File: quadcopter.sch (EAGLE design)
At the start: 69 parts, among them J1 AVR_SPI_PRG_6NS, U1 ATMEGA128RFA1, Y2 16MHz

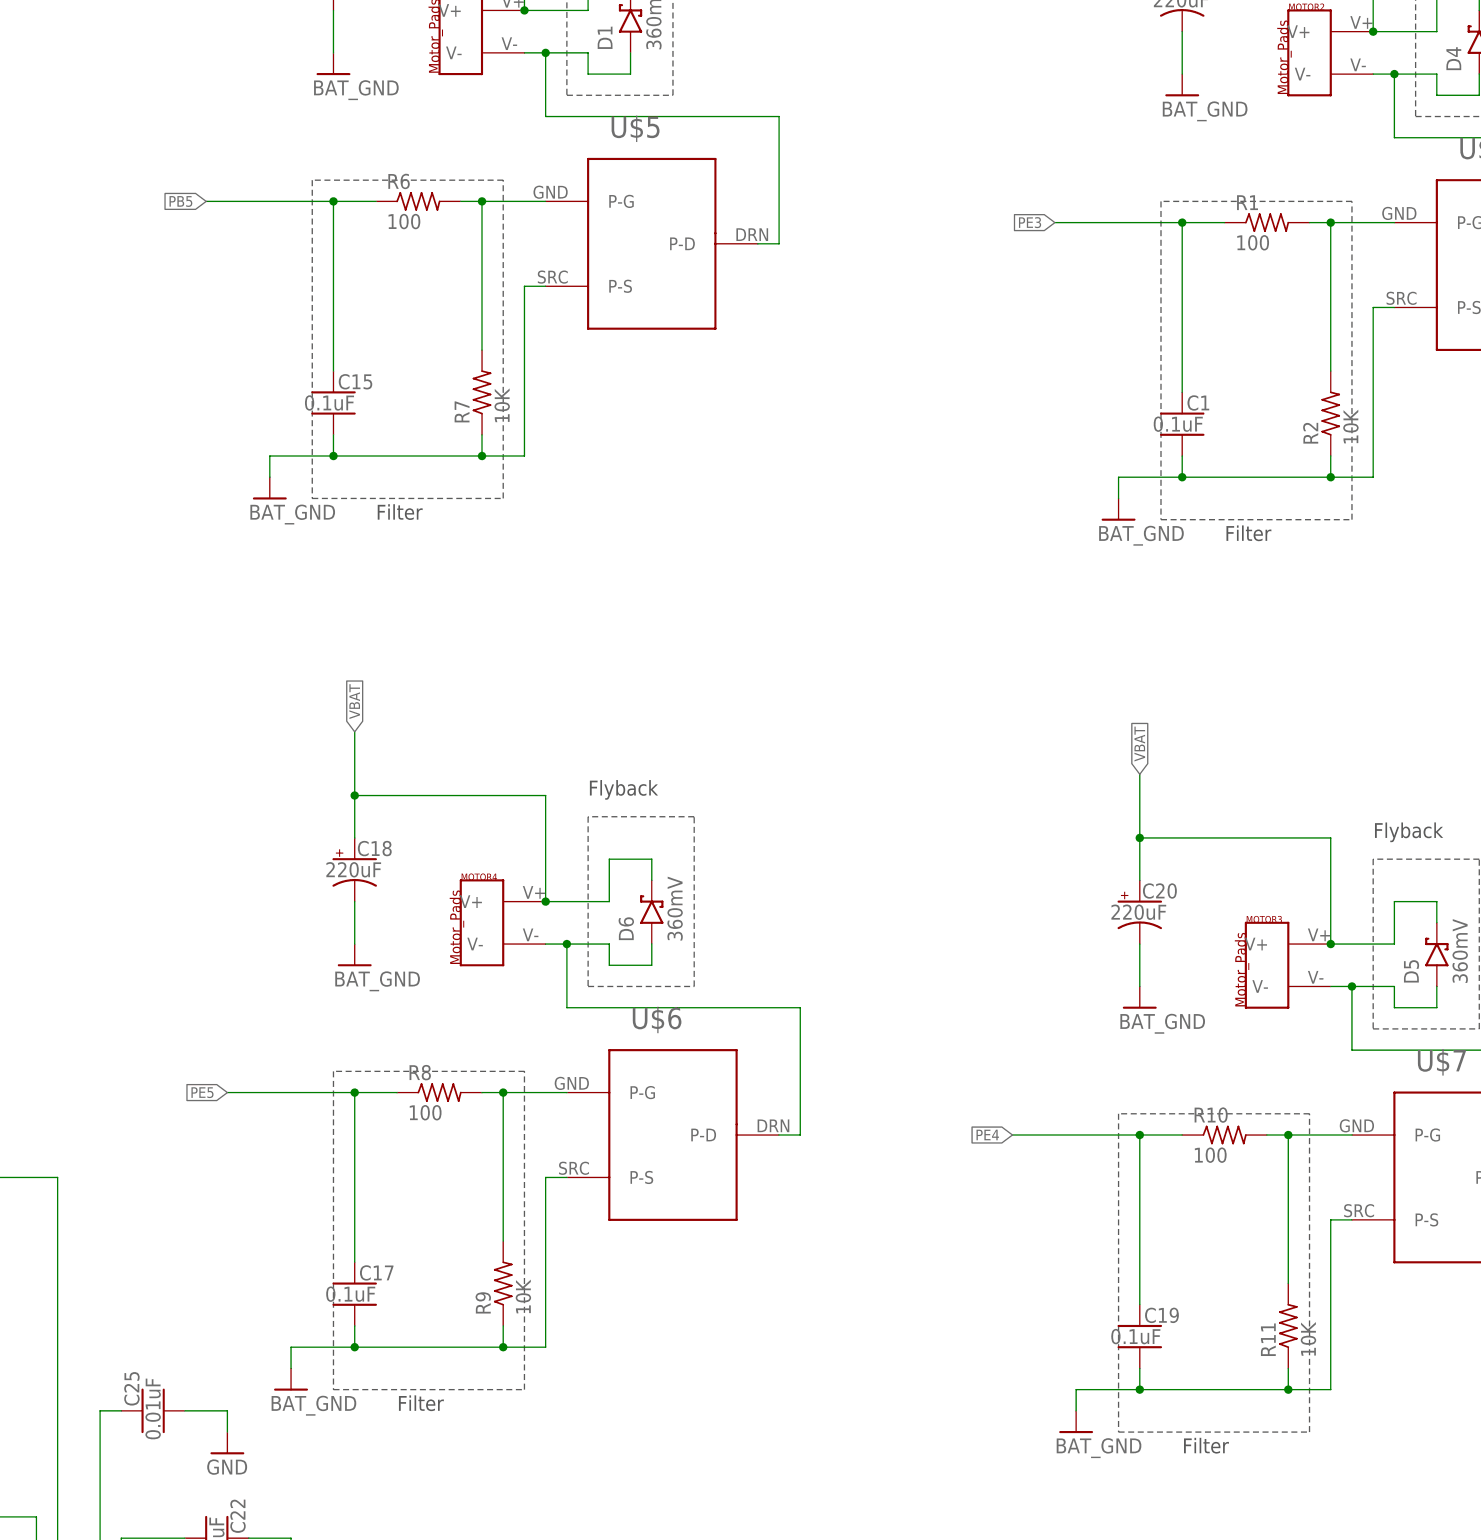
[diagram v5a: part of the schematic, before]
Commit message: Manually routed crystal, fixed motor driver filters.
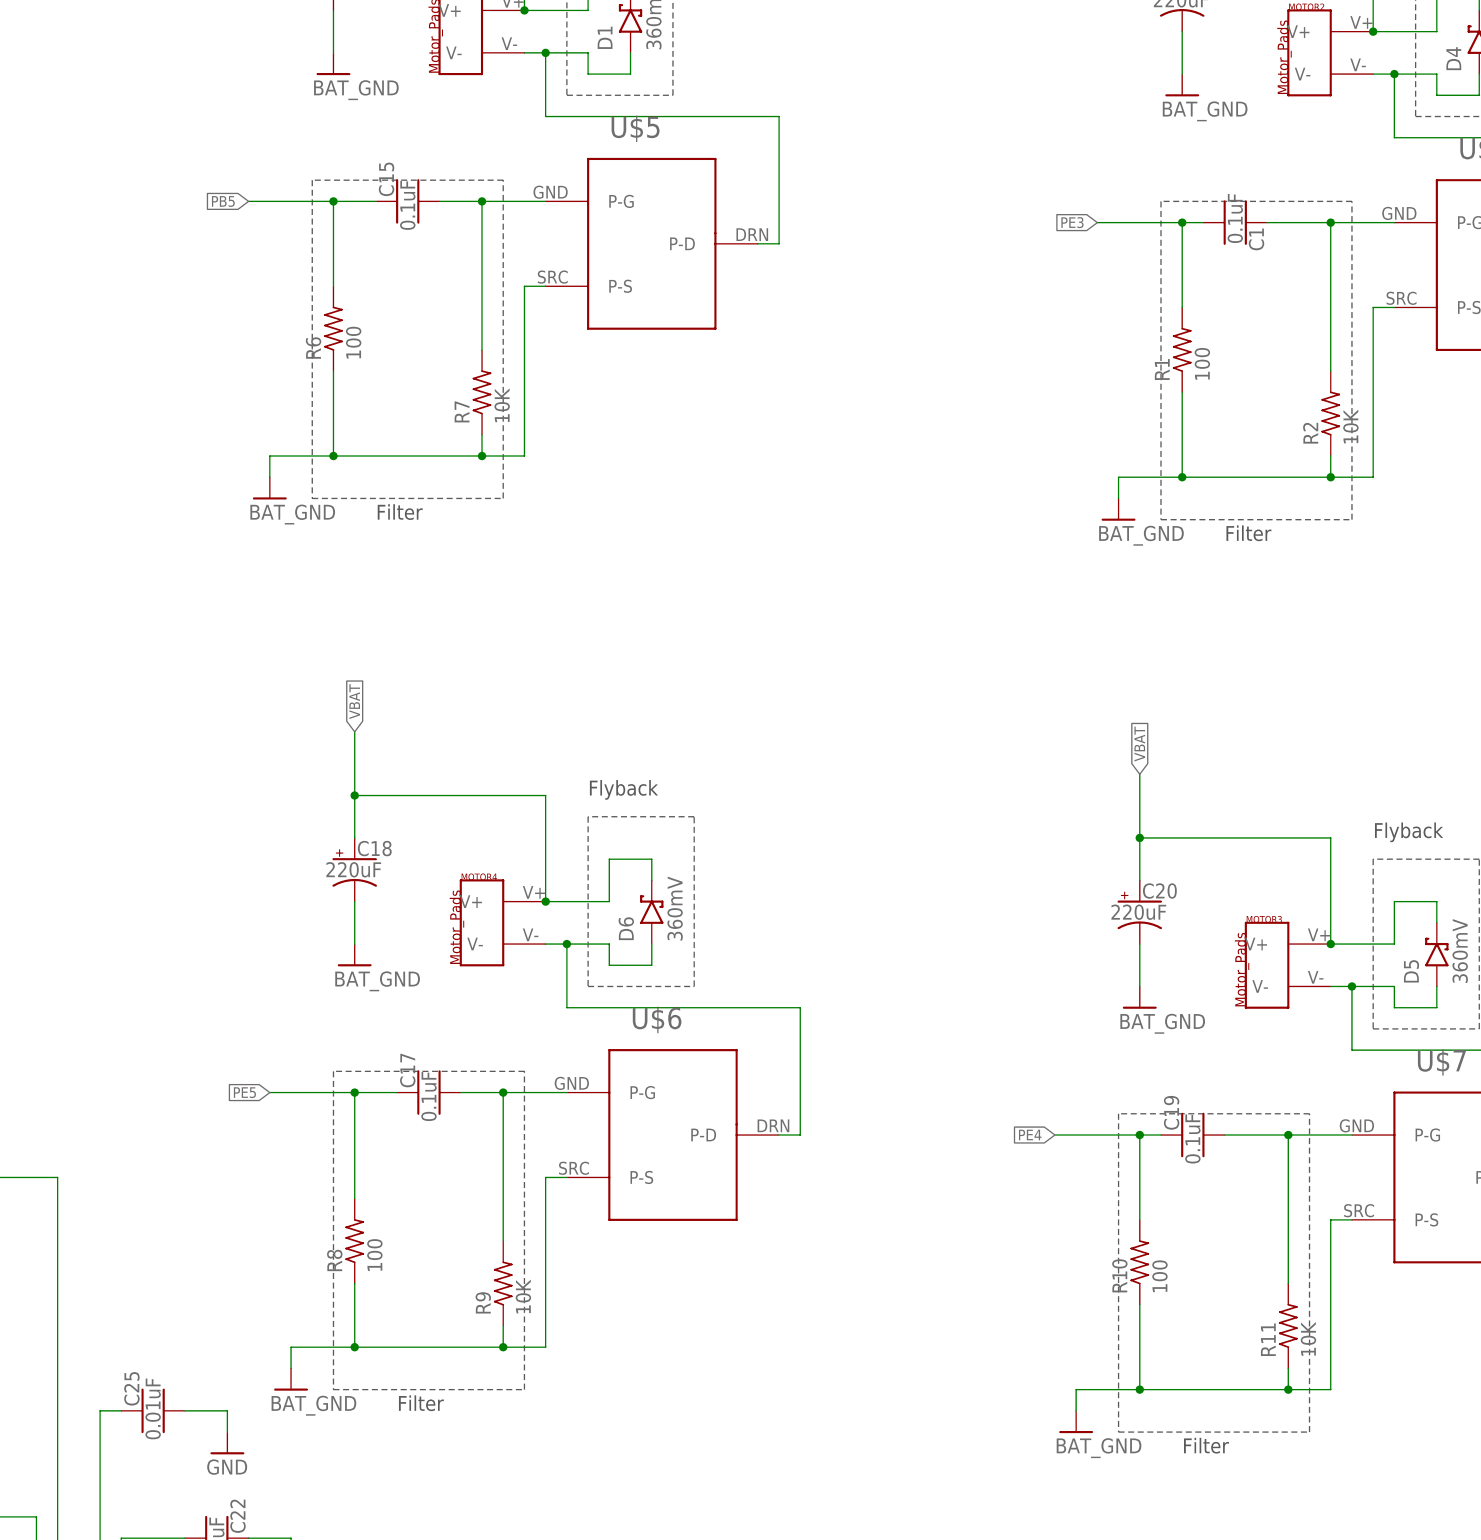
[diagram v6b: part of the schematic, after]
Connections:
- net BAT_GND: now also R1.1, R10.1, R6.1, R8.1; no longer C1.2, C15.2, C17.2, C19.2
- net FILTERED1: now also C15.2; no longer R6.2
- net FILTERED2: now also C1.1; no longer R1.2
- net FILTERED3: now also C19.2; no longer R10.2
- net FILTERED4: now also C17.2; no longer R8.2
- net PB5: now also R6.2; no longer R6.1
- net PE3: now also C1.2, R1.2; no longer C1.1, R1.1
- net PE4: now also R10.2; no longer R10.1
- net PE5: now also R8.2; no longer R8.1
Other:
- moved on the sheet: C1, C15, C17, C19, R1, R10, R6, R8
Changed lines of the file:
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@@
 </plain>
 <instances>
-<instance part="R1" gate="G$1" x="373.38" y="215.9"/>
+<instance part="R1" gate="G$1" x="363.22" y="200.66" rot="R90"/>
 <instance part="R2" gate="G$1" x="381" y="193.04" rot="R90"/>
 <instance part="GND1" gate="1" x="363.22" y="231.14"/>
@@
 <instance part="J2" gate="G$1" x="132.08" y="231.14"/>
 <instance part="J3" gate="G$1" x="63.5" y="251.46" rot="R270"/>
-<instance part="R6" gate="G$1" x="271.78" y="218.44"/>
+<instance part="R6" gate="G$1" x="261.62" y="203.2" rot="R90"/>
 <instance part="R7" gate="G$1" x="279.4" y="195.58" rot="R90"/>
 <instance part="GND27" gate="1" x="261.62" y="233.68"/>
@@
 <instance part="GND28" gate="1" x="254" y="182.88"/>
 <instance part="U$5" gate="G$1" x="299.72" y="213.36"/>
-<instance part="R8" gate="G$1" x="274.32" y="111.76"/>
+<instance part="R8" gate="G$1" x="264.16" y="93.98" rot="R90"/>
 <instance part="R9" gate="G$1" x="281.94" y="88.9" rot="R90"/>
 <instance part="GND29" gate="1" x="264.16" y="127"/>
@@
 <instance part="GND30" gate="1" x="256.54" y="76.2"/>
 <instance part="U$6" gate="G$1" x="302.26" y="106.68"/>
-<instance part="R10" gate="G$1" x="368.3" y="106.68"/>
+<instance part="R10" gate="G$1" x="358.14" y="91.44" rot="R90"/>
 <instance part="R11" gate="G$1" x="375.92" y="83.82" rot="R90"/>
 <instance part="GND31" gate="1" x="358.14" y="121.92"/>
@@
 <instance part="C25" gate="G$1" x="238.76" y="73.66" rot="R90"/>
 <instance part="C22" gate="G$1" x="248.92" y="58.42" rot="MR90"/>
-<instance part="C15" gate="G$1" x="261.62" y="195.58"/>
-<instance part="C1" gate="G$1" x="363.22" y="193.04"/>
-<instance part="C17" gate="G$1" x="264.16" y="88.9"/>
-<instance part="C19" gate="G$1" x="358.14" y="83.82"/>
+<instance part="C15" gate="G$1" x="269.24" y="218.44" rot="R90"/>
+<instance part="C1" gate="G$1" x="370.84" y="215.9" rot="R270"/>
+<instance part="C17" gate="G$1" x="271.78" y="111.76" rot="R90"/>
+<instance part="C19" gate="G$1" x="363.22" y="106.68" rot="R90"/>
 </instances>
 <busses>
@@
 <pinref part="R9" gate="G$1" pin="2"/>
 <wire x1="281.94" y1="93.98" x2="281.94" y2="111.76" width="0.1524" layer="91"/>
-<pinref part="R8" gate="G$1" pin="2"/>
-<wire x1="279.4" y1="111.76" x2="281.94" y2="111.76" width="0.1524" layer="91"/>
+<pinref part="C17" gate="G$1" pin="2"/>
+<wire x1="276.86" y1="111.76" x2="281.94" y2="111.76" width="0.1524" layer="91"/>
 <junction x="281.94" y="111.76"/>
 </segment>
@@
 </segment>
 <segment>
-<wire x1="261.62" y1="198.12" x2="261.62" y2="218.44" width="0.1524" layer="91"/>
-<pinref part="R6" gate="G$1" pin="1"/>
-<wire x1="266.7" y1="218.44" x2="261.62" y2="218.44" width="0.1524" layer="91"/>
+<pinref part="R6" gate="G$1" pin="2"/>
+<wire x1="261.62" y1="208.28" x2="261.62" y2="218.44" width="0.1524" layer="91"/>
+<pinref part="C15" gate="G$1" pin="1"/>
+<wire x1="261.62" y1="218.44" x2="266.7" y2="218.44" width="0.1524" layer="91"/>
+<wire x1="261.62" y1="218.44" x2="251.46" y2="218.44" width="0.1524" layer="91"/>
 <junction x="261.62" y="218.44"/>
-<wire x1="261.62" y1="218.44" x2="246.38" y2="218.44" width="0.1524" layer="91"/>
-<label x="246.38" y="218.44" size="1.27" layer="95" rot="R180" xref="yes"/>
-<pinref part="C15" gate="G$1" pin="1"/>
+<label x="251.46" y="218.44" size="1.27" layer="95" rot="R180" xref="yes"/>
 </segment>
 </net>
@@
 </segment>
 <segment>
-<wire x1="363.22" y1="195.58" x2="363.22" y2="215.9" width="0.1524" layer="91"/>
-<pinref part="R1" gate="G$1" pin="1"/>
-<wire x1="368.3" y1="215.9" x2="363.22" y2="215.9" width="0.1524" layer="91"/>
+<pinref part="R1" gate="G$1" pin="2"/>
+<wire x1="363.22" y1="205.74" x2="363.22" y2="215.9" width="0.1524" layer="91"/>
+<pinref part="C1" gate="G$1" pin="2"/>
+<wire x1="363.22" y1="215.9" x2="365.76" y2="215.9" width="0.1524" layer="91"/>
+<wire x1="363.22" y1="215.9" x2="353.06" y2="215.9" width="0.1524" layer="91"/>
 <junction x="363.22" y="215.9"/>
-<wire x1="363.22" y1="215.9" x2="347.98" y2="215.9" width="0.1524" layer="91"/>
-<label x="347.98" y="215.9" size="1.27" layer="95" rot="R180" xref="yes"/>
-<pinref part="C1" gate="G$1" pin="1"/>
+<label x="353.06" y="215.9" size="1.27" layer="95" rot="R180" xref="yes"/>
 </segment>
 </net>
@@
 </segment>
 <segment>
-<wire x1="358.14" y1="86.36" x2="358.14" y2="106.68" width="0.1524" layer="91"/>
-<pinref part="R10" gate="G$1" pin="1"/>
-<wire x1="363.22" y1="106.68" x2="358.14" y2="106.68" width="0.1524" layer="91"/>
+<pinref part="R10" gate="G$1" pin="2"/>
+<wire x1="358.14" y1="96.52" x2="358.14" y2="106.68" width="0.1524" layer="91"/>
+<pinref part="C19" gate="G$1" pin="1"/>
+<wire x1="358.14" y1="106.68" x2="360.68" y2="106.68" width="0.1524" layer="91"/>
+<wire x1="358.14" y1="106.68" x2="347.98" y2="106.68" width="0.1524" layer="91"/>
 <junction x="358.14" y="106.68"/>
-<wire x1="358.14" y1="106.68" x2="342.9" y2="106.68" width="0.1524" layer="91"/>
-<label x="342.9" y="106.68" size="1.27" layer="95" rot="R180" xref="yes"/>
-<pinref part="C19" gate="G$1" pin="1"/>
+<label x="347.98" y="106.68" size="1.27" layer="95" rot="R180" xref="yes"/>
 </segment>
 </net>
@@
 </segment>
 <segment>
-<wire x1="264.16" y1="91.44" x2="264.16" y2="111.76" width="0.1524" layer="91"/>
-<pinref part="R8" gate="G$1" pin="1"/>
+<pinref part="C17" gate="G$1" pin="1"/>
 <wire x1="269.24" y1="111.76" x2="264.16" y2="111.76" width="0.1524" layer="91"/>
+<pinref part="R8" gate="G$1" pin="2"/>
+<wire x1="264.16" y1="111.76" x2="254" y2="111.76" width="0.1524" layer="91"/>
+<wire x1="264.16" y1="111.76" x2="264.16" y2="99.06" width="0.1524" layer="91"/>
 <junction x="264.16" y="111.76"/>
-<wire x1="264.16" y1="111.76" x2="248.92" y2="111.76" width="0.1524" layer="91"/>
-<label x="248.92" y="111.76" size="1.27" layer="95" rot="R180" xref="yes"/>
-<pinref part="C17" gate="G$1" pin="1"/>
+<label x="254" y="111.76" size="1.27" layer="95" rot="R180" xref="yes"/>
 </segment>
 </net>
@@
 <pinref part="R9" gate="G$1" pin="1"/>
 <wire x1="281.94" y1="83.82" x2="281.94" y2="81.28" width="0.1524" layer="91"/>
-<wire x1="264.16" y1="81.28" x2="264.16" y2="83.82" width="0.1524" layer="91"/>
+<junction x="281.94" y="81.28"/>
+<pinref part="R8" gate="G$1" pin="1"/>
+<wire x1="264.16" y1="88.9" x2="264.16" y2="81.28" width="0.1524" layer="91"/>
 <junction x="264.16" y="81.28"/>
-<pinref part="C17" gate="G$1" pin="2"/>
-<junction x="281.94" y="81.28"/>
 </segment>
 <segment>
@@
 <pinref part="R7" gate="G$1" pin="1"/>
 <wire x1="279.4" y1="190.5" x2="279.4" y2="187.96" width="0.1524" layer="91"/>
-<wire x1="261.62" y1="187.96" x2="261.62" y2="190.5" width="0.1524" layer="91"/>
+<junction x="279.4" y="187.96"/>
+<pinref part="R6" gate="G$1" pin="1"/>
+<wire x1="261.62" y1="198.12" x2="261.62" y2="187.96" width="0.1524" layer="91"/>
 <junction x="261.62" y="187.96"/>
-<pinref part="C15" gate="G$1" pin="2"/>
-<junction x="279.4" y="187.96"/>
 </segment>
 <segment>
@@
 <pinref part="R11" gate="G$1" pin="1"/>
 <wire x1="375.92" y1="78.74" x2="375.92" y2="76.2" width="0.1524" layer="91"/>
-<wire x1="358.14" y1="76.2" x2="358.14" y2="78.74" width="0.1524" layer="91"/>
+<junction x="375.92" y="76.2"/>
+<pinref part="R10" gate="G$1" pin="1"/>
+<wire x1="358.14" y1="86.36" x2="358.14" y2="76.2" width="0.1524" layer="91"/>
 <junction x="358.14" y="76.2"/>
-<pinref part="C19" gate="G$1" pin="2"/>
-<junction x="375.92" y="76.2"/>
 </segment>
 <segment>
@@
 <pinref part="R2" gate="G$1" pin="1"/>
 <wire x1="381" y1="187.96" x2="381" y2="185.42" width="0.1524" layer="91"/>
-<wire x1="363.22" y1="185.42" x2="363.22" y2="187.96" width="0.1524" layer="91"/>
+<junction x="381" y="185.42"/>
+<pinref part="R1" gate="G$1" pin="1"/>
+<wire x1="363.22" y1="195.58" x2="363.22" y2="185.42" width="0.1524" layer="91"/>
 <junction x="363.22" y="185.42"/>
-<pinref part="C1" gate="G$1" pin="2"/>
-<junction x="381" y="185.42"/>
 </segment>
 <segment>
@@
 <pinref part="R7" gate="G$1" pin="2"/>
 <wire x1="279.4" y1="200.66" x2="279.4" y2="218.44" width="0.1524" layer="91"/>
-<pinref part="R6" gate="G$1" pin="2"/>
-<wire x1="276.86" y1="218.44" x2="279.4" y2="218.44" width="0.1524" layer="91"/>
+<pinref part="C15" gate="G$1" pin="2"/>
+<wire x1="274.32" y1="218.44" x2="279.4" y2="218.44" width="0.1524" layer="91"/>
 <junction x="279.4" y="218.44"/>
 </segment>
@@
 <pinref part="R2" gate="G$1" pin="2"/>
 <wire x1="381" y1="198.12" x2="381" y2="215.9" width="0.1524" layer="91"/>
-<pinref part="R1" gate="G$1" pin="2"/>
-<wire x1="378.46" y1="215.9" x2="381" y2="215.9" width="0.1524" layer="91"/>
+<pinref part="C1" gate="G$1" pin="1"/>
+<wire x1="373.38" y1="215.9" x2="381" y2="215.9" width="0.1524" layer="91"/>
 <junction x="381" y="215.9"/>
 </segment>
@@
 <pinref part="R11" gate="G$1" pin="2"/>
 <wire x1="375.92" y1="88.9" x2="375.92" y2="106.68" width="0.1524" layer="91"/>
-<pinref part="R10" gate="G$1" pin="2"/>
-<wire x1="373.38" y1="106.68" x2="375.92" y2="106.68" width="0.1524" layer="91"/>
+<pinref part="C19" gate="G$1" pin="2"/>
+<wire x1="368.3" y1="106.68" x2="375.92" y2="106.68" width="0.1524" layer="91"/>
 <junction x="375.92" y="106.68"/>
 </segment>

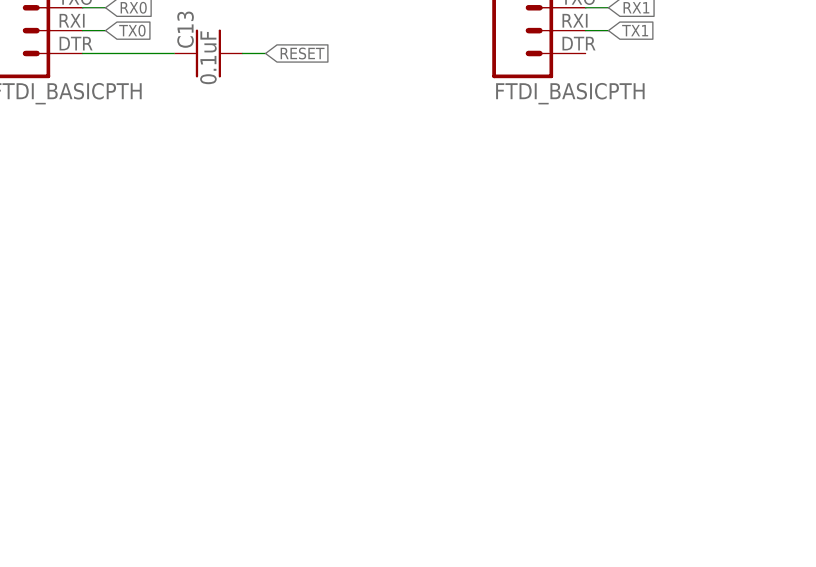
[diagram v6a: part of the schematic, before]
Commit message: Fixed issues found by Swanson's review, board ready to be auto-routed
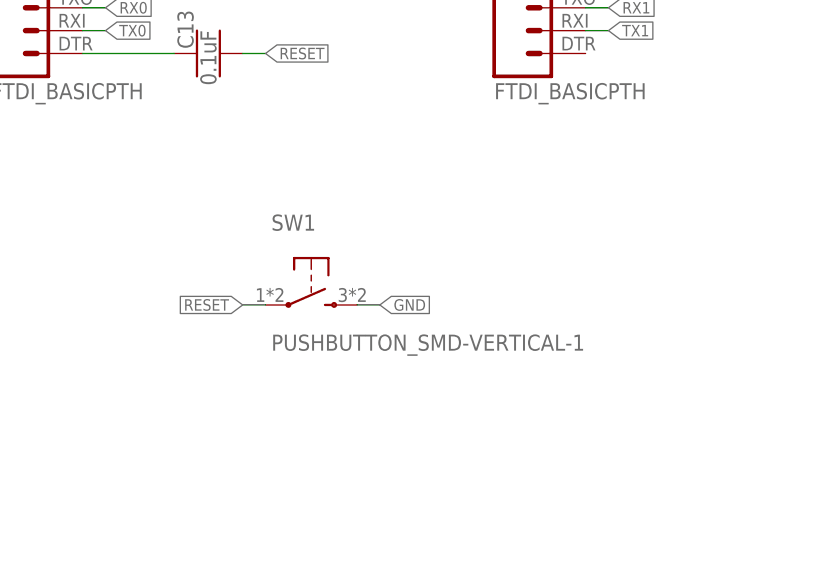
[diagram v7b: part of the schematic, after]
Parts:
- added SW1: PUSHBUTTON_SMD-VERTICAL-1, quadparts_prebuilt:PUSHBUTTON_SMD-VERTICAL-1
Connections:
- net GND: now also SW1.2
- net RESET: now also SW1.1
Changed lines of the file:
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@@
 <part name="C17" library="quadparts_prebuilt" deviceset="CAPACITOR-NP_" device="SMD-2012-0805_CERAMIC-0.1UF" value="0.1uF"/>
 <part name="C19" library="quadparts_prebuilt" deviceset="CAPACITOR-NP_" device="SMD-2012-0805_CERAMIC-0.1UF" value="0.1uF"/>
+<part name="SW1" library="quadparts_prebuilt" deviceset="PUSHBUTTON_" device="SMD-VERTICAL-1"/>
 </parts>
 <sheets>
@@
 <instance part="C17" gate="G$1" x="271.78" y="111.76" rot="R90"/>
 <instance part="C19" gate="G$1" x="363.22" y="106.68" rot="R90"/>
+<instance part="SW1" gate="G$1" x="170.18" y="172.72"/>
 </instances>
 <busses>
@@
 <wire x1="33.02" y1="241.3" x2="33.02" y2="238.76" width="0.1524" layer="91"/>
 </segment>
+<segment>
+<pinref part="SW1" gate="G$1" pin="2"/>
+<wire x1="175.26" y1="170.18" x2="177.8" y2="170.18" width="0.1524" layer="91"/>
+<label x="177.8" y="170.18" size="1.27" layer="95" xref="yes"/>
+</segment>
 </net>
 <net name="FILTERED4" class="2">
@@
 <label x="175.26" y="241.3" size="1.27" layer="95" rot="R180" xref="yes"/>
 </segment>
-</net>
+<segment>
+<pinref part="SW1" gate="G$1" pin="1"/>
+<wire x1="165.1" y1="170.18" x2="162.56" y2="170.18" width="0.1524" layer="91"/>
+<label x="162.56" y="170.18" size="1.27" layer="95" rot="R180" xref="yes"/>
+</segment>
+</net>
